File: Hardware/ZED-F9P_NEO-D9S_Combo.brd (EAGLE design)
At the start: 43.2 x 63.5 mm, 174 parts, among them J1 ANTENNA-SMA-GROUNDEDEDGE_SMA, J2 Qwiic Right Angle, J3 USB Female Type C Connector, J4 Qwiic Right Angle, J6 USB Female Type C Connector, U1 U-BLOX_NEO-D9S-00B, U2 3.3V, U3 POWER-DIVIDER, U4 U-BLOX_ZED-F9P

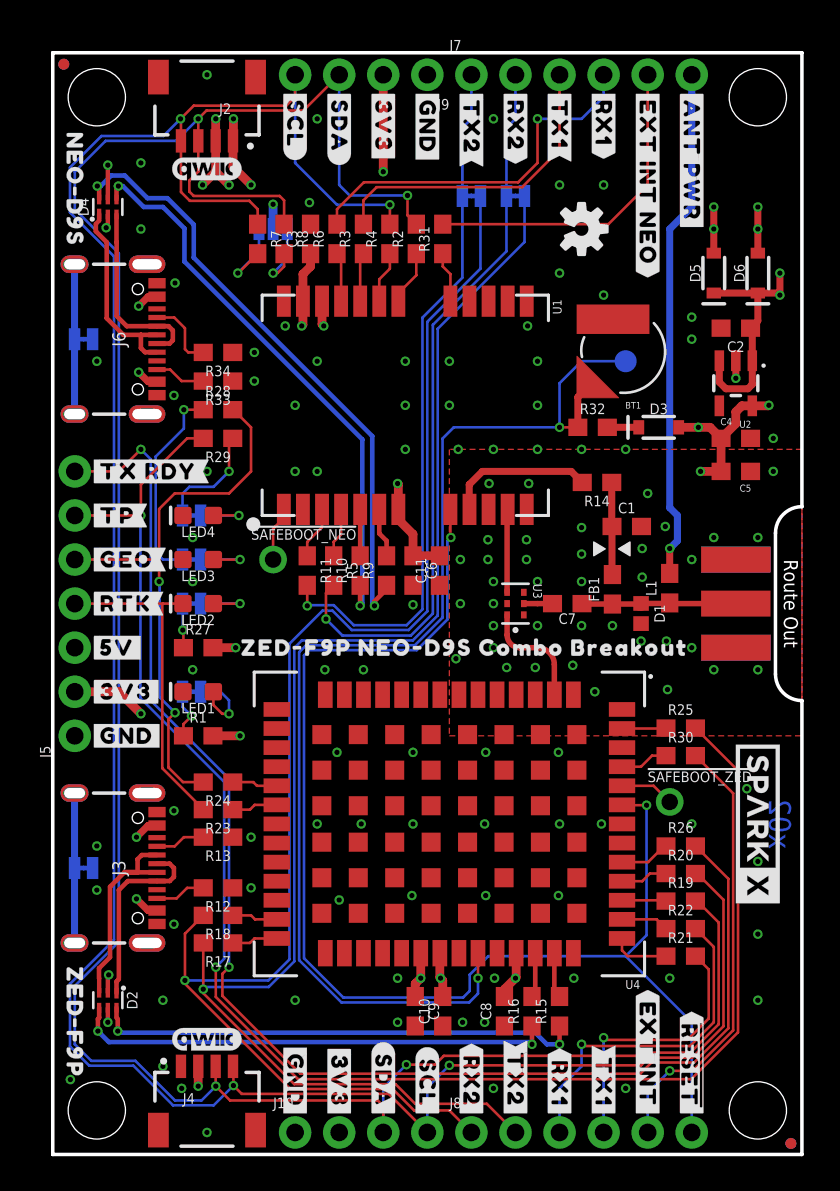
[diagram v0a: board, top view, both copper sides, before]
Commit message: Updates various text and symbols
* Replaces ESD Diodes and Antenna Splitter Diode with larger packages
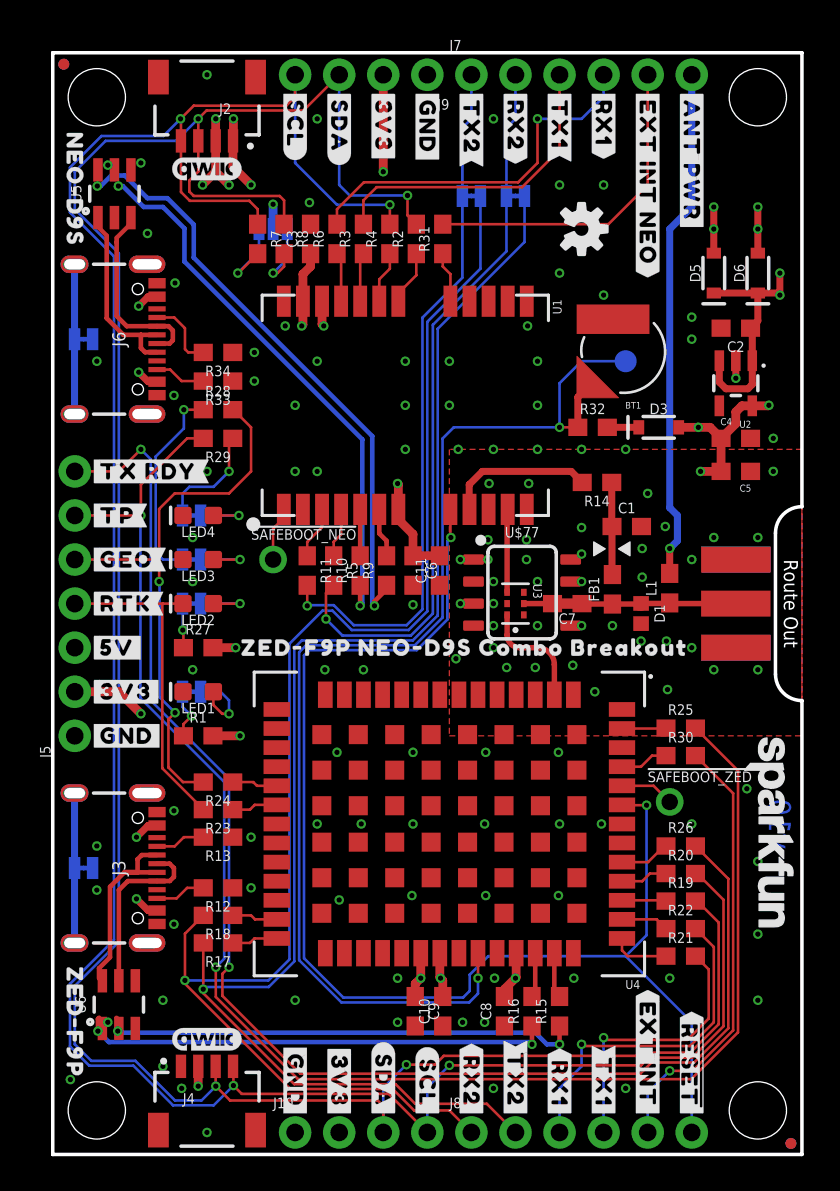
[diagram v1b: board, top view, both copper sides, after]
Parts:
- removed D2, D4: PRTR5V0U2F, SparkFun-IC-Power:SOT886
- removed U$78: SPARKX-LOGO4, SparkX:SPARKX-MEDIUM
- added LOGO2: SFE_LOGO_NAME.1_INCH, SparkFun-Aesthetics:SFE_LOGO_NAME_.1
- added U5, U6: ESD Diode, SparkFun-DiscreteSemi:SOT-23-6
- R1: value 1k -> 4.7k
- U$77: value SPARKX-LOGO4 -> BP2G1+_POWER_SPLITTER; device SparkX:SPARKX-MEDIUM -> SparkFun-RF:XX21
- moved U$77 19.0 mm to (27.1, 32.4)
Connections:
- net ANT: now also U$77.2
- net ANT_NEO: now also U$77.8
- net ANT_ZED: now also U$77.5
- net D+_NEO: now also U5.6; no longer D4.6
- net D+_ZED: now also U6.6; no longer D2.6
- net D-_NEO: now also U5.4; no longer D4.4
- net D-_ZED: now also U6.4; no longer D2.4
- net GND: now also U$77.1, U$77.3, U$77.4, U$77.6, U$77.7, U5.2, U6.2; no longer D2.2, D4.2
- net USB_D+: now also U6.1; no longer D2.1
- net USB_D+1: now also U5.1; no longer D4.1
- net USB_D-: now also U6.3; no longer D2.3
- net USB_D-1: now also U5.3; no longer D4.3
- net V_USB: now also U6.5; no longer D2.5
- net V_USB_2: now also U5.5; no longer D4.5
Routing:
- net V_USB_2: track 63.7 -> 61.7 mm
- net GND: track 7.12 -> 5.26 mm, vias 126 -> 124
- net V_USB: track 92.6 -> 91.8 mm
- net USB_D-: track 11.4 -> 10.6 mm
- net D-_NEO: track 32.9 -> 32.2 mm
- net D+_NEO: track 35.6 -> 34.9 mm
- net USB_D+: track 11.1 -> 10.4 mm
- net D-_ZED: track 27.8 -> 27.2 mm
- net D+_ZED: track 28.2 -> 27.6 mm
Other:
- board text added: "v10"
- board text removed: "x02"

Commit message: Changes 90 Ohm impedance calculation to decrease trace width
* Adds additional measures
* Updates silk
* Adds polygons to USB shield
* Adds four layer numbers
* Updated ordering instructions
* Routes new antenna splitter
* Spaces out some of the more common transmission traces, UART and I2C, to minimize cross talk
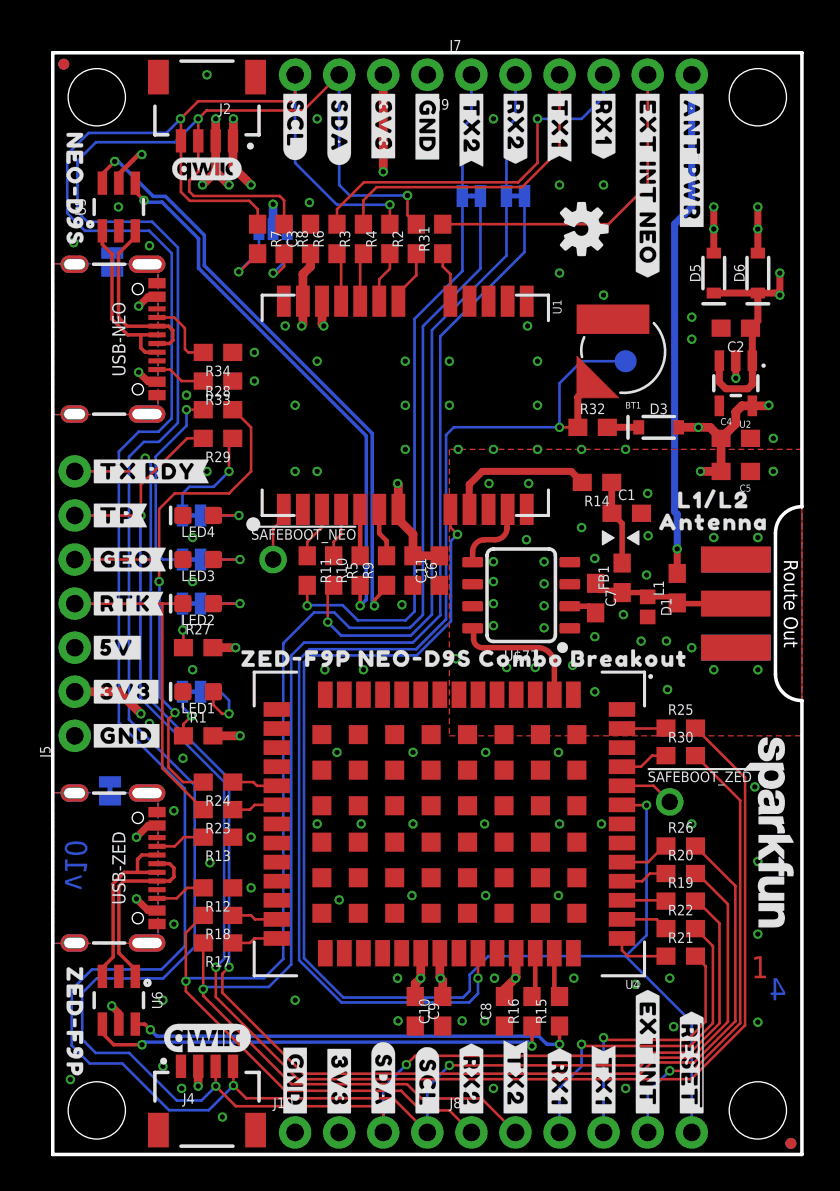
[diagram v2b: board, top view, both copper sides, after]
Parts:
- removed U$14: (no value), SparkFun-Aesthetics:QWIIC_4MM
- removed U$76: (no value), output:V_BKCP0
- removed U3: POWER-DIVIDER, SparkFun-RF:PD0922J5050S2HF_ANA
- added LOGO3: QWIIC_LOGO_5MM, SparkFun-Aesthetics:QWIIC_5MM
- added U$78: (no value), top:ZED#F9P16
- U$33: device output:OPEN_JUMPERS_TO0 -> top:L1#L218
- U$53: device output:#SHLD#0 -> top:#SHLD_NEO#12
- U$54: device output:ISOLATE_UART21 -> top:ANTENNA18
- U$55: device output:NEO#D9S0 -> top:NEO#D9S16
- U$64: device output:ZED#F9P0 -> top:COMBO16
- U$67: device output:COMBO10 -> top:BREAKOUT17
- U$68: device output:BREAKOUT11 -> SparkFun-Aesthetics:SFE_LOGO_NAME_.2
- U$7: device output:#SHLD#0 -> top:#SHLD_ZED#15
- U$71: device output:#SAFEBOOT#_NEO0 -> top:##SAFEBOOT#_NEO#13
- U$72: device output:#SAFEBOOT#_ZED0 -> top:##SAFEBOOT#_ZED#14
- moved U$7 31.1 mm to (3.30, 15.9)
- moved U$53 29.7 mm to (3.43, 46.2)
- moved LOGO4 20.2 mm to (6.10, 2.54)
- moved U$68 17.3 mm to (30.5, 31.9)
- moved U$54 15.9 mm to (38.1, 36.4), flipped to the top, turned to 0 degrees
- moved U$73 15.3 mm to (15.2, 31.8)
- moved U$74 15.3 mm to (16.6, 31.9)
- moved U$33 13.2 mm to (38.1, 37.7), flipped to the top, turned to 0 degrees
- moved U$55 10.7 mm to (24.4, 31.9)
- moved U$64 10.4 mm to (22.5, 31.9)
- moved U$67 10.4 mm to (20.3, 31.9)
- moved U$71 6.60 mm to (12.7, 41.3)
- moved U$72 6.48 mm to (35.6, 27.2)
- moved SHLD_NEO 4.74 mm to (3.43, 51.4), turned to 270 degrees
- moved SHLD_ZED 4.70 mm to (3.30, 21.0), turned to 270 degrees
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- renumbered J3 to USB-ZED, J6 to USB-NEO
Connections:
- net ANT: no longer U3.2
- net ANT_NEO: now also U$77.5; no longer U$77.8, U3.4
- net ANT_ZED: now also U$77.8; no longer U$77.5, U3.6
- net GND: no longer U3.1, U3.3, U3.5
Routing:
- net SCL: track 146.6 -> 158.7 mm
- net SDA: track 147.5 -> 157.7 mm
- net SHIELD_NEO: track 17.0 -> 8.36 mm
- net SHIELD_ZED: track 17.0 -> 8.36 mm
- net V_USB_2: track 61.7 -> 64.8 mm
- net V_USB: track 91.8 -> 93.5 mm
- net D+_ZED: track 27.6 -> 26.0 mm
- net ANT_ZED: track 6.32 -> 7.64 mm
- net USB_D+1: track 11.4 -> 10.1 mm
- net USB_D-1: track 11.2 -> 10.4 mm
- net ANT_NEO: track 4.79 -> 4.23 mm
- net GND: vias 124 -> 120
- added copper zone on layer 1, net SHIELD_NEO
- added copper zone on layer 16, net SHIELD_NEO
- added copper zone on layer 1, net SHIELD_ZED
- added copper zone on layer 16, net SHIELD_ZED
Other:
- board text added: "1"
- board text added: "1.6mm Thickness 4-Layers 1oz Copper 0.5oz Inner Copper Stackup: JLC7628 Material: TG135-140 Lead-Free HASL finish Red soldermask White silkscreen"
- board text added: "2"
- board text added: "3"
- board text added: "4"
- board text added: "Revised By: Elias Santistevan"
- board text removed: "1.6mm Thickness 4-Layers 1oz copper Lead-Free HASL finish Black soldermask White silkscreen"

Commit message: Fixes ESD diode
* Adds L-Band text/silk to relevant Antenna notes
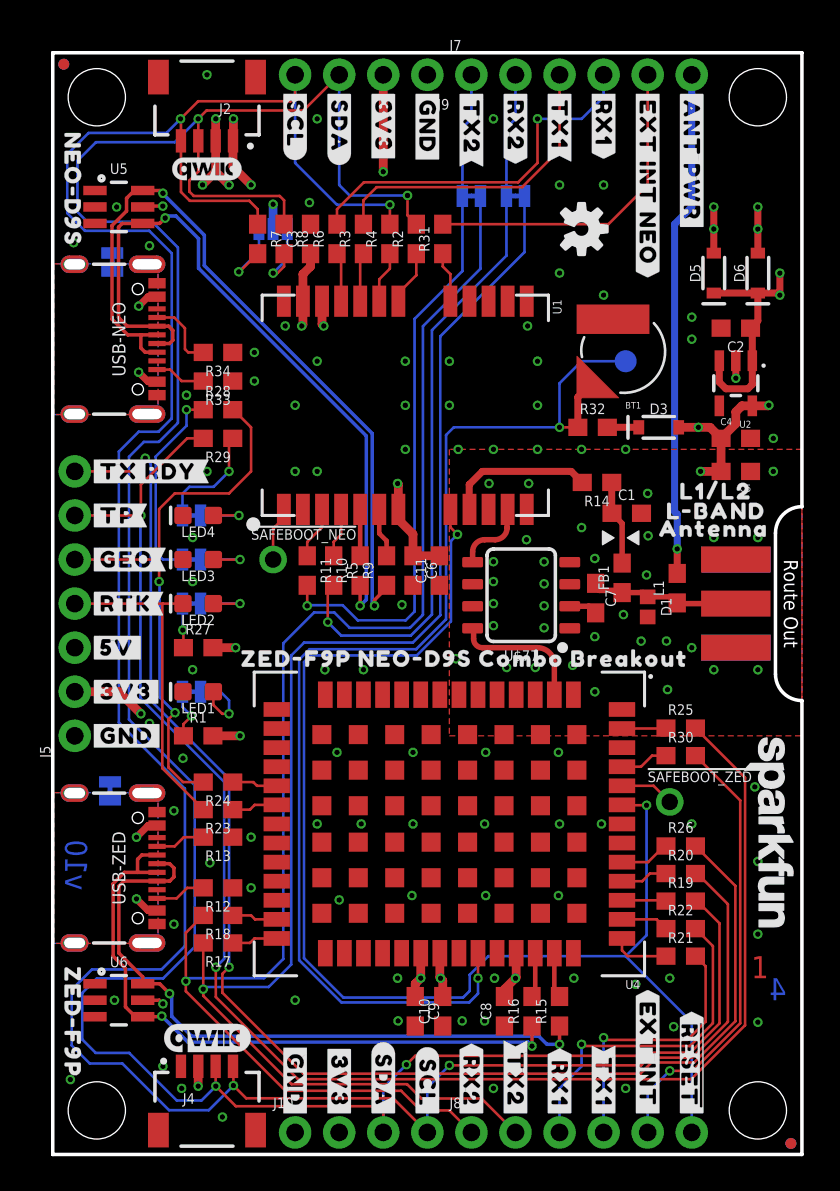
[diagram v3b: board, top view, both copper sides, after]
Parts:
- added U$14: (no value), top:L#BAND18
- moved U$33 0.52 mm to (38.2, 38.2)
- moved U$54 0.38 mm to (38.1, 36.1)
- moved U$65 0.13 mm to (1.14, 7.62)
- moved U$66 0.13 mm to (1.14, 55.6)
- turned U5 to 270 degrees
- turned U6 to 270 degrees
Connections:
- removed net USB_D+: U6.1, USB-ZED.A6, USB-ZED.B6
- removed net USB_D+1: U5.1, USB-NEO.A6, USB-NEO.B6
- removed net USB_D-: U6.3, USB-ZED.A7, USB-ZED.B7
- removed net USB_D-1: U5.3, USB-NEO.A7, USB-NEO.B7
- net D+_NEO: now also USB-NEO.A6, USB-NEO.B6
- net D+_ZED: now also USB-ZED.A6, USB-ZED.B6
- net D-_NEO: now also USB-NEO.A7, USB-NEO.B7
- net D-_ZED: now also USB-ZED.A7, USB-ZED.B7
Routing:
- net D+_ZED: track 26.0 -> 38.4 mm
- net D-_ZED: track 26.9 -> 37.7 mm
- net USB_D+: track 10.6 -> 0.00 mm
- net USB_D-1: track 10.4 -> 0.00 mm
- net USB_D-: track 10.4 -> 0.00 mm
- net D-_NEO: track 31.8 -> 42.1 mm
- net USB_D+1: track 10.1 -> 0.00 mm
- net D+_NEO: track 35.4 -> 44.7 mm
- net V_USB_2: track 64.8 -> 67.5 mm
- net V_USB: track 93.5 -> 94.3 mm

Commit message: Re-adds UART text on UART Jumpers
* Updates the default address text so it's not so wordy.
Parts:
- added U$76: (no value), top:DEF_ADDRESS#_12
- added U$79: (no value), top:NEO#D9S#13
- added U$80: (no value), top:ZED#F9P#13
- added U$81: (no value), top:0X4313
- added U$82: (no value), top:0X4213
- U$73: device output:NEO#D9S_DEF_ADDR#_0X4310 -> top:OPEN_JUMPERS13
- U$74: device output:ZED#F9P_DEF_ADDR#_0X420 -> top:TO_ISOLATE_UART214
- moved U$73 20.4 mm to (22.2, 50.9)
- moved U$74 19.5 mm to (20.8, 50.9)
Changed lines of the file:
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@@
 <element name="U$69" library="output" package="#PWR#0" value="" x="8.89" y="26.67" smashed="yes" rot="MR0"/>
 <element name="U$70" library="output" package="#3V3#4" value="" x="2.032" y="26.67" smashed="yes" rot="MR0"/>
-<element name="U$73" library="output" package="NEO#D9S_DEF_ADDR#_0X4310" value="" x="15.24" y="31.75" smashed="yes" rot="MR90"/>
-<element name="U$74" library="output" package="ZED#F9P_DEF_ADDR#_0X420" value="" x="16.637" y="31.877" smashed="yes" rot="MR90"/>
 <element name="U$48" library="output" package="#EXT_INT_ZED#0" value="" x="34.29" y="2.032" smashed="yes" rot="MR90"/>
 <element name="U$75" library="output" package="ZED#F9P_NEO#D9S_COMBO_BREAKOUT0" value="" x="23.749" y="28.575" smashed="yes"/>
@@
 <element name="LOGO3" library="SparkFun-Aesthetics" package="QWIIC_5MM" value="QWIIC_LOGO_5MM" x="8.89" y="6.731" smashed="yes"/>
 <element name="U$14" library="top" package="L#BAND18" value="" x="38.227" y="37.084" smashed="yes"/>
+<element name="U$73" library="top" package="OPEN_JUMPERS13" value="" x="22.225" y="50.927" smashed="yes" rot="MR90"/>
+<element name="U$74" library="top" package="TO_ISOLATE_UART214" value="" x="20.828" y="50.927" smashed="yes" rot="MR90"/>
+<element name="U$76" library="top" package="DEF_ADDRESS#_12" value="" x="8.89" y="53.34" smashed="yes" rot="MR90"/>
+<element name="U$79" library="top" package="NEO#D9S#13" value="" x="7.62" y="51.054" smashed="yes" rot="MR90"/>
+<element name="U$80" library="top" package="ZED#F9P#13" value="" x="6.35" y="51.181" smashed="yes" rot="MR90"/>
+<element name="U$81" library="top" package="0X4313" value="" x="7.62" y="56.769" smashed="yes" rot="MR90"/>
+<element name="U$82" library="top" package="0X4213" value="" x="6.35" y="56.769" smashed="yes" rot="MR90"/>
 </elements>
 <signals>
@@
 <wire x1="34.0436" y1="32.3859" x2="34.29" y2="32.1395" width="0.3175" layer="1"/>
 <wire x1="34.0436" y1="32.3859" x2="32.8168" y2="32.3859" width="0.3175" layer="1"/>
-<wire x1="32.8168" y1="32.3859" x2="32.6907" y2="32.512" width="0.3175" layer="1"/>
-<wire x1="32.6907" y1="32.512" x2="31.496" y2="32.512" width="0.3175" layer="1"/>
-<wire x1="31.496" y1="32.512" x2="31.2928" y2="32.7152" width="0.3175" layer="1"/>
+<wire x1="32.8168" y1="32.3859" x2="32.5637" y2="32.639" width="0.3175" layer="1"/>
+<wire x1="32.5637" y1="32.639" x2="31.369" y2="32.639" width="0.3175" layer="1"/>
+<wire x1="31.369" y1="32.639" x2="31.2928" y2="32.7152" width="0.3175" layer="1"/>
 <wire x1="31.2928" y1="32.7152" x2="31.2928" y2="32.9175" width="0.3175" layer="1"/>
 <wire x1="34.29" y1="32.1395" x2="34.290003125" y2="32.1395" width="0.2667" layer="1"/>
-<wire x1="34.29" y1="32.1395" x2="34.290003125" y2="32.1395" width="0.2667" layer="1"/>
-</signal>
+</signal>

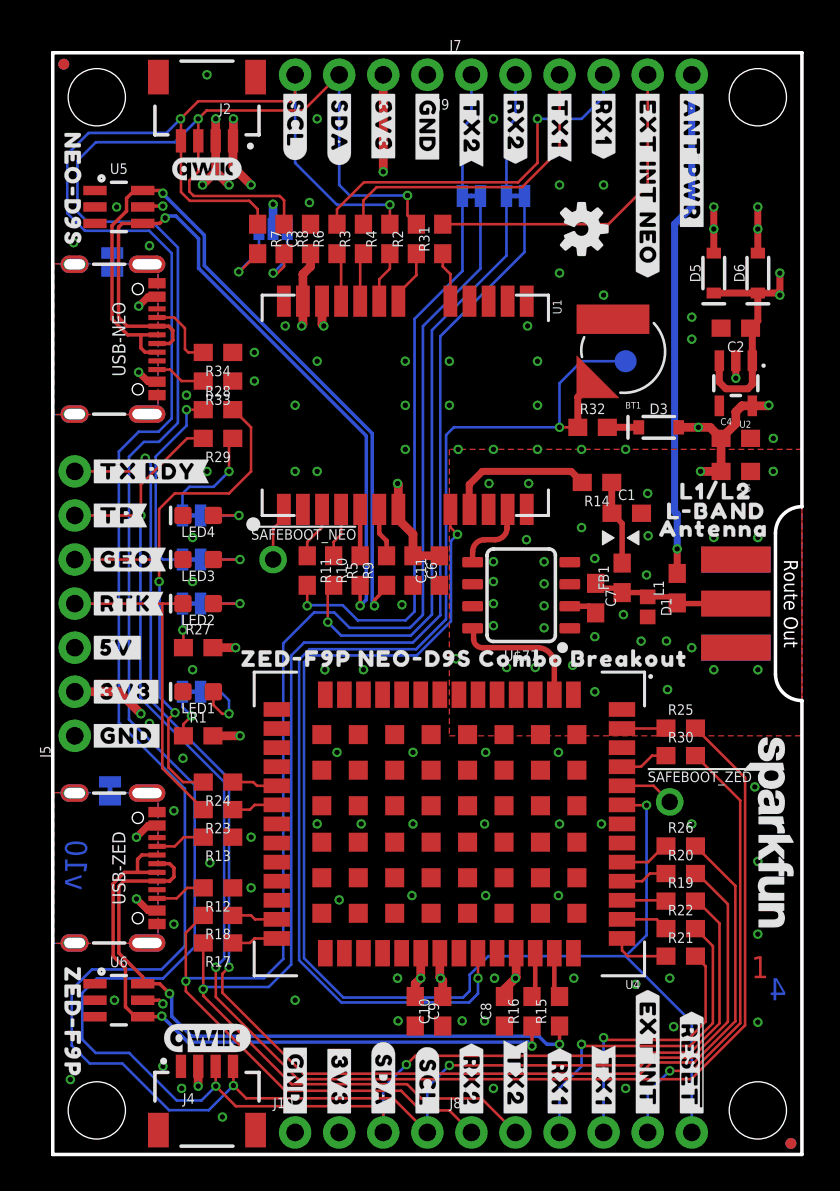
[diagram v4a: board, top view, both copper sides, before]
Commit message: Normalizes the drill sizes
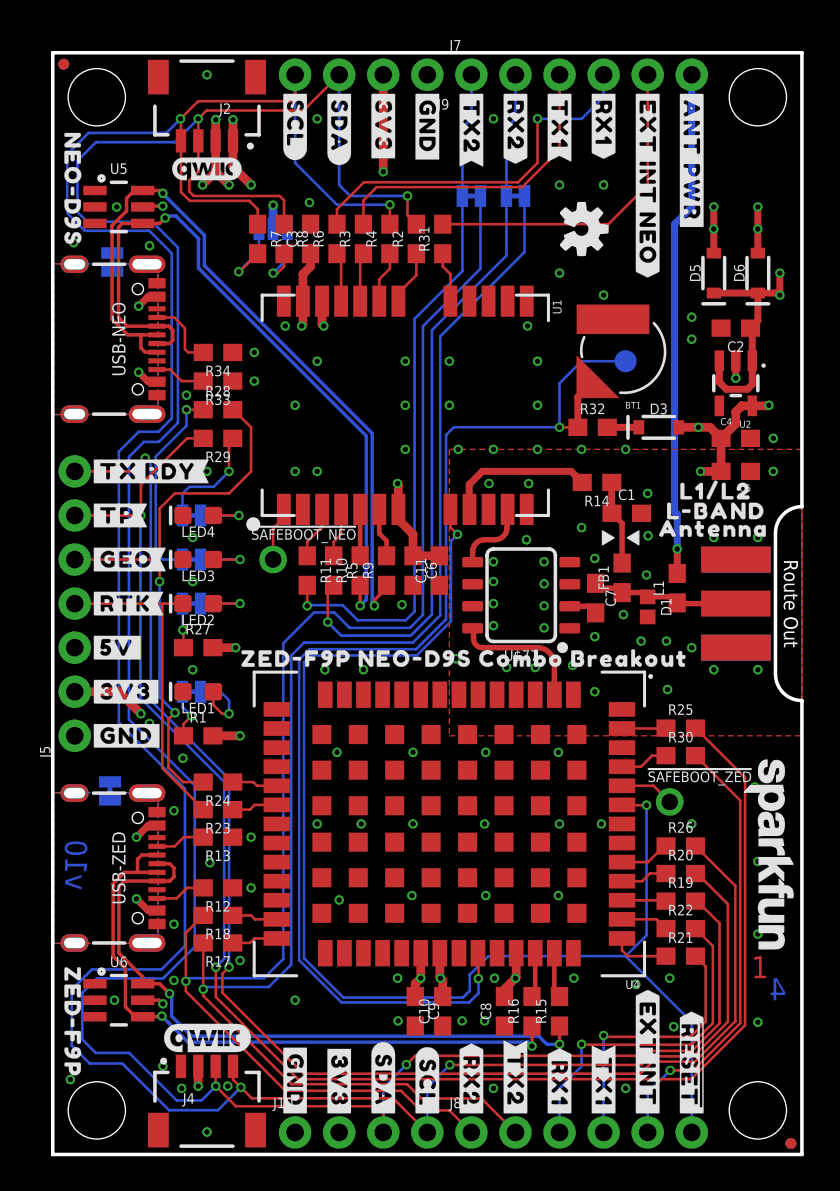
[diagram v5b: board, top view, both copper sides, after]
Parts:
- moved LOGO2 1.27 mm to (41.3, 17.3)
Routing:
- net GND: track 5.26 -> 5.20 mm, vias 120 -> 123
